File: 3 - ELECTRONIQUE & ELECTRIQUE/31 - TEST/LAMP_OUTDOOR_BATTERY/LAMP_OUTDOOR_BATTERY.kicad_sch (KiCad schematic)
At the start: 13 parts, among them J1 629722000214, U1 MCP73833-FCI_UN, U2 MT3608

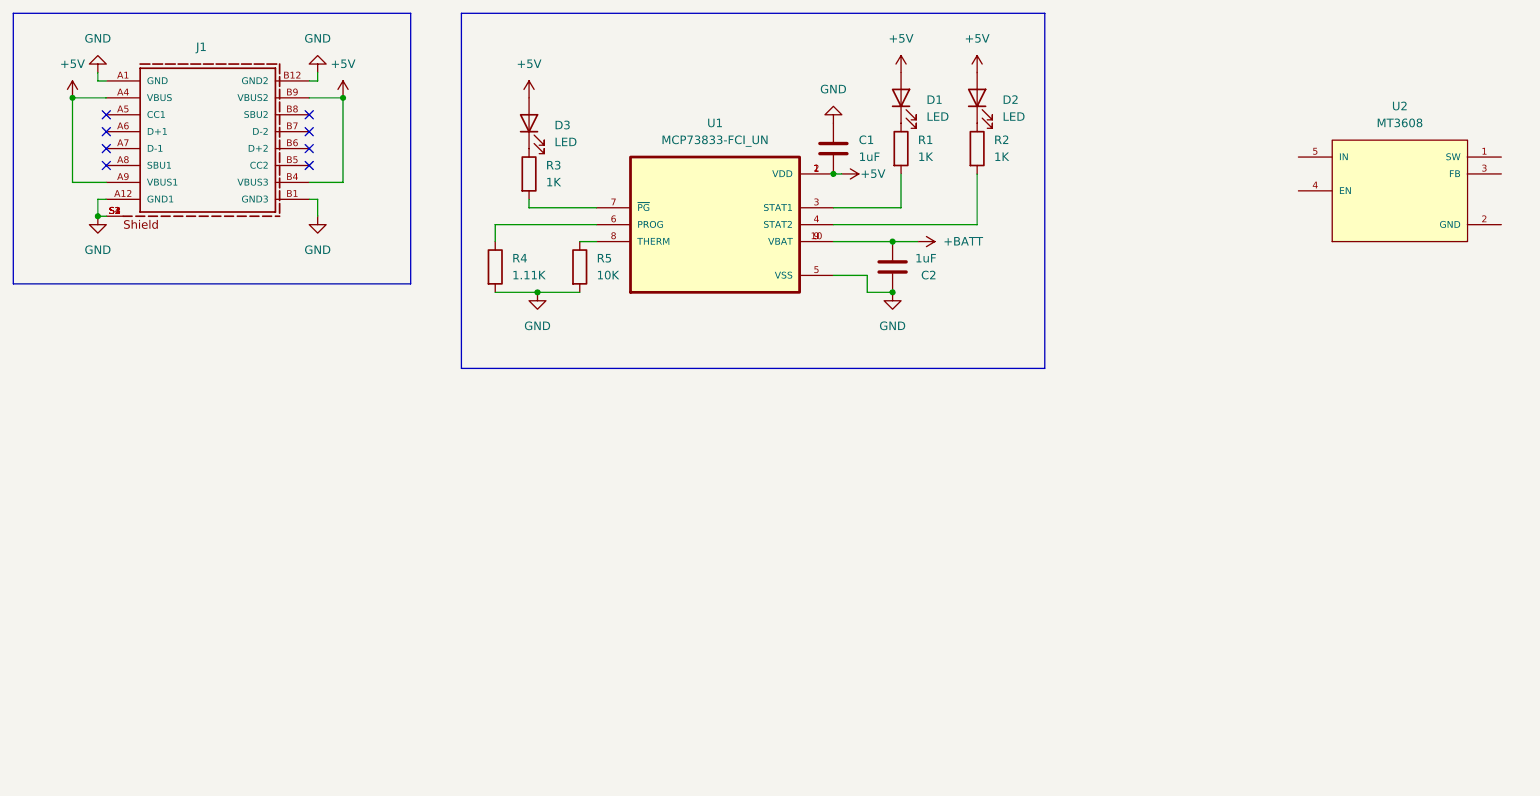
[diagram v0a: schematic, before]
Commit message: Boost converter circuit
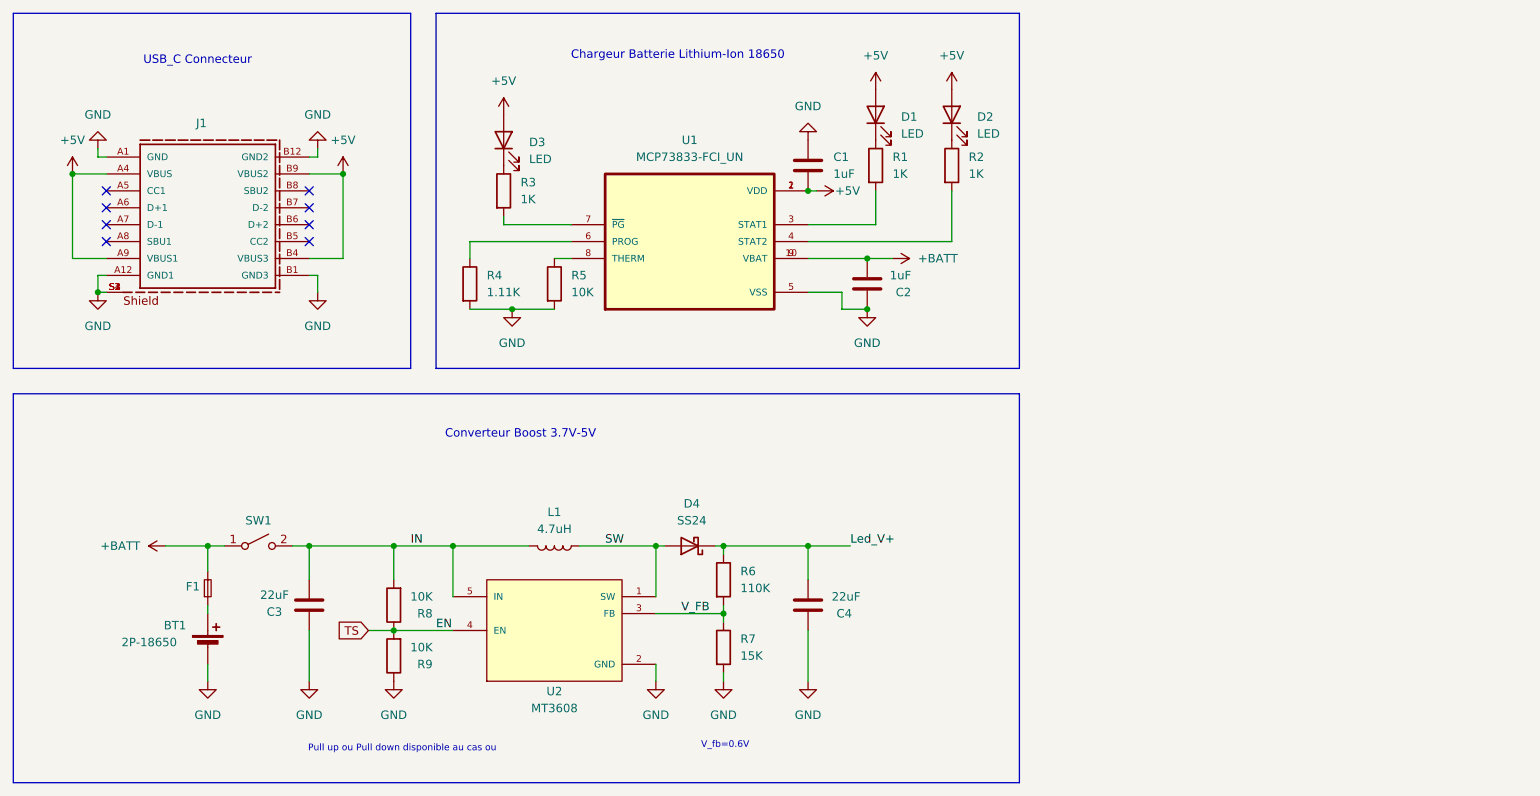
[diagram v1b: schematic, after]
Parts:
- added BT1: 2P-18650, symbol Device:Battery_Cell
- added C3, C4: 22uF, Capacitor_SMD:C_0402_1005Metric_Pad0.74x0.62mm_HandSolder, symbol Device:C
- added D4: SS24, Diode_SMD:D_SMA, symbol Diode:SS24
- added F1: Fuse_Small, Fuse:Fuse_1206_3216Metric_Pad1.42x1.75mm_HandSolder, symbol Device:Fuse_Small
- added L1: 4.7uH, symbol Device:L
- added R6: 110K, Resistor_SMD:R_0402_1005Metric_Pad0.72x0.64mm_HandSolder, symbol Device:R
- added R7: 15K, Resistor_SMD:R_0402_1005Metric_Pad0.72x0.64mm_HandSolder, symbol Device:R
- added R8, R9: 10K, Resistor_SMD:R_0402_1005Metric_Pad0.72x0.64mm_HandSolder, symbol Device:R
- added SW1: SW_SPST, Connector_PinHeader_2.54mm:PinHeader_1x02_P2.54mm_Vertical, symbol Switch:SW_SPST
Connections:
- net +BATT: now also F1.2, SW1.1 (A)
- net GND: now also U2.2 (GND), BT1.2 (-), C3.1, C4.1, R7.2, R9.1
- net SW: now reaches U2.1 (SW)
- net SW: now also D4.2 (A), L1.1
- net V_FB: now reaches U2.3 (FB)
- net V_FB: now also R6.2, R7.1
- net TS: now reaches U2.4 (EN)
- net TS: now also R8.1, R9.2
- net IN: now reaches U2.5 (IN)
- net IN: now also C3.2, L1.2, R8.2, SW1.2 (B)
- new net: BT1.1 (+), F1.1
- new net Led_V+: C4.2, D4.1 (K), R6.1
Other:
- note added: "Chargeur Batterie Lithium-Ion 18650"
- note added: "Converteur Boost 3.7V-5V"
- note added: "Pull up ou Pull down disponible au cas ou"
- note added: "USB_C Connecteur"
- note added: "V_fb=0.6V"
- moved on the sheet: C1, C2, D1, D2, D3, J1, R1, R2, R3, R4, R5, U1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

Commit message: Import des symboles et empreintes
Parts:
- added U3: AT42QT1012-MAHR, LAMP_OUTDOOR_BATTERY:SON50P200X200X60-9N, symbol LAMP_OUTDOOR_BATTERY:AT42QT1012-MAHR
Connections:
- new net: U3.2 (NC), U3.3 (NC)
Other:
- note added: "Convertisseur Boost 3.7V-5V"
- note removed: "Converteur Boost 3.7V-5V"
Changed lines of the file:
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@@
 		)
 	)
-	(text "Converteur Boost 3.7V-5V"
+	(text "Convertisseur Boost 3.7V-5V"
 		(exclude_from_sim no)
 		(at 101.6 87.376 0)
@@
 					(unit 1)
 				)
+			)
+		)
+	)
+	(symbol
+		(lib_id "LAMP_OUTDOOR_BATTERY:AT42QT1012-MAHR")
+		(at 237.49 50.8 0)
+		(unit 1)
+		(exclude_from_sim no)
+		(in_bom yes)
+		(on_board yes)
+		(dnp no)
+		(fields_autoplaced yes)
+		(property "Reference" "U3"
+			(at 237.49 33.02 0)
+			(effects
+				(font
+					(size 1.27 1.27)
+				)
+			)
+		)
+		(property "Value" "AT42QT1012-MAHR"
+			(at 237.49 35.56 0)
+			(effects
+				(font
+					(size 1.27 1.27)
+				)
+			)
+		)
+		(property "Footprint" "LAMP_OUTDOOR_BATTERY:SON50P200X200X60-9N"
+			(at 237.49 50.8 0)
+			(effects
+				(font
+					(size 1.27 1.27)
+				)
+				(justify bottom)
+				(hide yes)
+			)
+		)
+		(property "Datasheet" ""
+			(at 237.49 50.8 0)
+			(effects
+				(font
+					(size 1.27 1.27)
+				)
+				(hide yes)
+			)
+		)
+		(property "Description" ""
+			(at 237.49 50.8 0)
+			(effects
+				(font
+					(size 1.27 1.27)
+				)
+				(hide yes)
+			)
+		)
+		(property "MF" "Microchip Technology"
+			(at 237.49 50.8 0)
+			(effects
+				(font
+					(size 1.27 1.27)
+				)
+				(justify bottom)
+				(hide yes)
+			)
+		)
+		(property "SNAPEDA_PACKAGE_ID" "10574"
+			(at 237.49 50.8 0)
+			(effects
+				(font
+					(size 1.27 1.27)
+				)
+				(justify bottom)
+				(hide yes)
+			)
+		)
+		(property "MAXIMUM_PACKAGE_HEIGHT" "0.6mm"
+			(at 237.49 50.8 0)
+			(effects
+				(font
+					(size 1.27 1.27)
+				)
+				(justify bottom)
+				(hide yes)
+			)
+		)
+		(property "Price" "None"
+			(at 237.49 50.8 0)
+			(effects
+				(font
+					(size 1.27 1.27)
+				)
+				(justify bottom)
+				(hide yes)
+			)
+		)
+		(property "Package" "UDFN-8 Microchip"
+			(at 237.49 50.8 0)
+			(effects
+				(font
+					(size 1.27 1.27)
+				)
+				(justify bottom)
+				(hide yes)
+			)
+		)
+		(property "Check_prices" "https://www.snapeda.com/parts/AT42QT1012-MAHR/Microchip/view-part/?ref=eda"
+			(at 237.49 50.8 0)
+			(effects
+				(font
+					(size 1.27 1.27)
+				)
+				(justify bottom)
+				(hide yes)
+			)
+		)
+		(property "STANDARD" "IPC 7351B"
+			(at 237.49 50.8 0)
+			(effects
+				(font
+					(size 1.27 1.27)
+				)
+				(justify bottom)
+				(hide yes)
+			)
+		)
+		(property "PARTREV" "I"
+			(at 237.49 50.8 0)
+			(effects
+				(font
+					(size 1.27 1.27)
+				)
+				(justify bottom)
+				(hide yes)
+			)
+		)
+		(property "SnapEDA_Link" "https://www.snapeda.com/parts/AT42QT1012-MAHR/Microchip/view-part/?ref=snap"
+			(at 237.49 50.8 0)
+			(effects
+				(font
+					(size 1.27 1.27)
+				)
+				(justify bottom)
+				(hide yes)
+			)
+		)
+		(property "MP" "AT42QT1012-MAHR"
+			(at 237.49 50.8 0)
+			(effects
+				(font
+					(size 1.27 1.27)
+				)
+				(justify bottom)
+				(hide yes)
+			)
+		)
+		(property "Description_1" "\n                        \n                            Capacitive Touch Screen 1 Key 8-Pin UDFN EP T/R\n                        \n"
+			(at 237.49 50.8 0)
+			(effects
+				(font
+					(size 1.27 1.27)
+				)
+				(justify bottom)
+				(hide yes)
+			)
+		)
+		(property "MANUFACTURER" "Microchip"
+			(at 237.49 50.8 0)
+			(effects
+				(font
+					(size 1.27 1.27)
+				)
+				(justify bottom)
+				(hide yes)
+			)
+		)
+		(property "Availability" "In Stock"
+			(at 237.49 50.8 0)
+			(effects
+				(font
+					(size 1.27 1.27)
+				)
+				(justify bottom)
+				(hide yes)
+			)
+		)
+		(property "SNAPEDA_PN" "AT42QT1012-MAHR"
+			(at 237.49 50.8 0)
+			(effects
+				(font
+					(size 1.27 1.27)
+				)
+				(justify bottom)
+				(hide yes)
+			)
+		)
+		(pin "6"
+		)
+		(pin "9"
+		)
+		(pin "1"
+		)
+		(pin "4"
+		)
+		(pin "5"
+		)
+		(pin "2"
+		)
+		(pin "7"
+		)
+		(pin "8"
+		)
+		(pin "3"
+		)
+		(instances
+			(project ""
+				(path "/77872c89-7cd3-4b01-8286-04ddd44a2a11"
+					(reference "U3")
+					(unit 1)
+				)
